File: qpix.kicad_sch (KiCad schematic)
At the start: 90 parts, among them J1 Conn_01x40, J13 DigReset, J2 Conn_01x09, J3 Conn_02x03, J4 Conn_02x03, J5 SPI, J6 Conn_02x03, J8 Conn_02x03, J9 Conn_Coaxial_Power, Q1 Q_NMOS_GSD, Q2 Q_NMOS_GSD, Q3 Q_NMOS_GSD, Q4 Q_NMOS_GSD, U1 qpix_digital

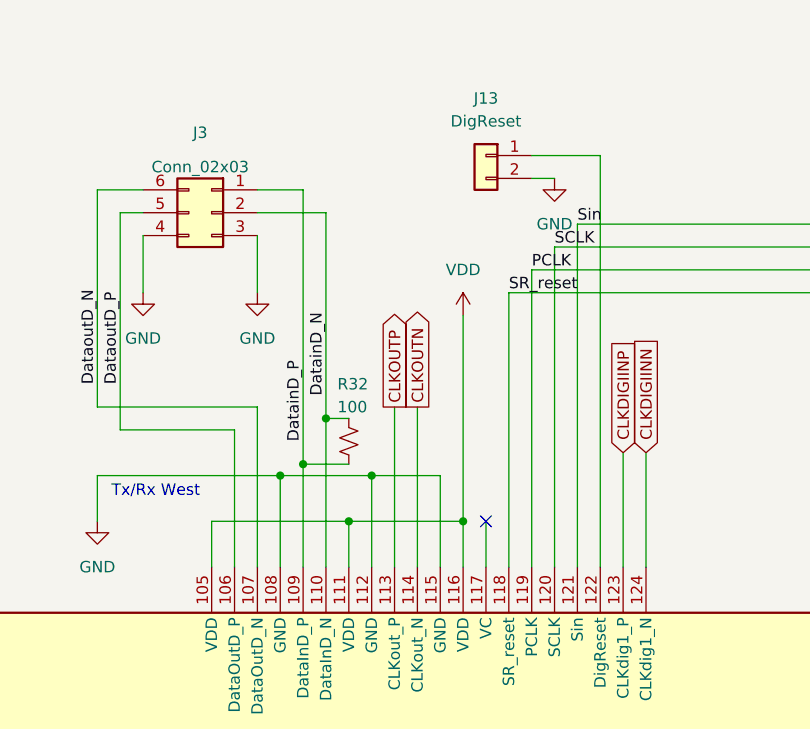
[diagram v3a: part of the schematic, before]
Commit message: connect VC DAC reference voltage to the pin header
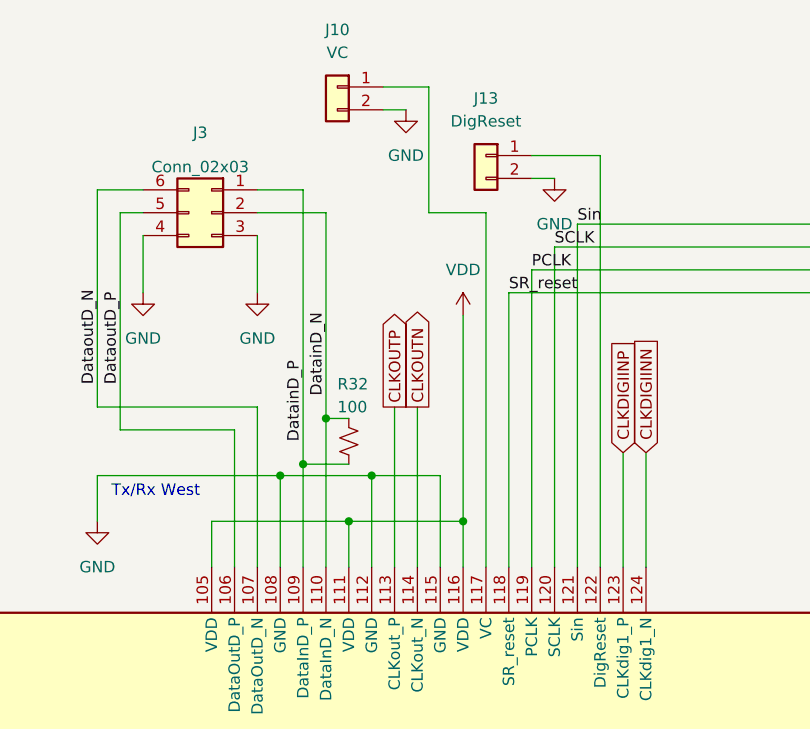
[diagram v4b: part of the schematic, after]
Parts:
- added J10: VC, Connector_PinHeader_2.54mm:PinHeader_1x02_P2.54mm_Vertical, symbol Connector_Generic:Conn_01x02
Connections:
- net GND: now also J10.2 (Pin_2)
- net at U1.117 (VC): now also J10.1 (Pin_1)
- no-connect marks 1 -> 0
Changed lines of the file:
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@@
   (junction (at 356.87 54.61) (diameter 0) (color 0 0 0 0)
   )
-  (no_connect (at 195.58 72.39))
   (wire (pts (xy 250.19 110.49) (xy 250.19 123.19))
     (stroke (width 0) (type default) (color 0 0 0 0))
@@
     (stroke (width 0) (type default) (color 0 0 0 0))
   )
+  (wire (pts (xy 184.15 26.67) (xy 186.69 26.67))
+    (stroke (width 0) (type default) (color 0 0 0 0))
+  )
   (polyline (pts (xy 276.86 104.14) (xy 406.4 104.14))
     (stroke (width 0) (type default) (color 0 0 0 0))
@@
     (stroke (width 0) (type default) (color 0 0 0 0))
   )
+  (wire (pts (xy 189.23 38.1) (xy 189.23 24.13))
+    (stroke (width 0) (type default) (color 0 0 0 0))
+  )
   (wire (pts (xy 231.14 269.24) (xy 227.33 269.24))
     (stroke (width 0) (type default) (color 0 0 0 0))
@@
     (stroke (width 0) (type default) (color 0 0 0 0))
   )
-  (wire (pts (xy 195.58 72.39) (xy 195.58 77.47))
+  (wire (pts (xy 195.58 38.1) (xy 195.58 77.47))
     (stroke (width 0) (type default) (color 0 0 0 0))
   )
@@
     (stroke (width 0) (type default) (color 0 0 0 0))
   )
+  (wire (pts (xy 195.58 38.1) (xy 189.23 38.1))
+    (stroke (width 0) (type default) (color 0 0 0 0))
+  )
   (wire (pts (xy 208.28 242.57) (xy 208.28 250.19))
     (stroke (width 0) (type default) (color 0 0 0 0))
@@
     (stroke (width 0) (type default) (color 0 0 0 0))
   )
+  (wire (pts (xy 189.23 24.13) (xy 184.15 24.13))
+    (stroke (width 0) (type default) (color 0 0 0 0))
+  )
   (wire (pts (xy 243.84 115.57) (xy 280.67 115.57))
     (stroke (width 0) (type default) (color 0 0 0 0))
@@
     (pin "2")
   )
+  (symbol (lib_id "power:GND") (at 186.69 26.67 0) (unit 1)
+    (in_bom yes) (on_board yes) (fields_autoplaced)
+    (property "Reference" "#PWR030" (id 0) (at 186.69 33.02 0)
+      (effects (font (size 1.27 1.27)) hide)
+    )
+    (property "Value" "GND" (id 1) (at 186.69 31.75 0))
+    (property "Footprint" "" (id 2) (at 186.69 26.67 0)
+      (effects (font (size 1.27 1.27)) hide)
+    )
+    (property "Datasheet" "" (id 3) (at 186.69 26.67 0)
+      (effects (font (size 1.27 1.27)) hide)
+    )
+    (pin "1")
+  )
   (symbol (lib_id "power:GND") (at 63.5 100.33 0) (unit 1)
     (in_bom yes) (on_board yes) (fields_autoplaced)
@@
     (pin "1")
   )
+  (symbol (lib_id "Connector_Generic:Conn_01x02") (at 179.07 24.13 0) (mirror y) (unit 1)
+    (in_bom yes) (on_board yes) (fields_autoplaced)
+    (property "Reference" "J10" (id 0) (at 179.07 17.78 0))
+    (property "Value" "VC" (id 1) (at 179.07 20.32 0))
+    (property "Footprint" "Connector_PinHeader_2.54mm:PinHeader_1x02_P2.54mm_Vertical" (id 2) (at 179.07 24.13 0)
+      (effects (font (size 1.27 1.27)) hide)
+    )
+    (property "Datasheet" "~" (id 3) (at 179.07 24.13 0)
+      (effects (font (size 1.27 1.27)) hide)
+    )
+    (pin "1")
+    (pin "2")
+  )
   (symbol (lib_id "Device:R_US") (at 392.43 38.1 0) (unit 1)
     (in_bom yes) (on_board yes) (fields_autoplaced)
@@
       (reference "#PWR029") (unit 1) (value "GND") (footprint "")
     )
+    (path "/7bcc8bd1-e233-4082-9758-fb375cb15776"
+      (reference "#PWR030") (unit 1) (value "GND") (footprint "")
+    )
     (path "/cfd9746d-22ce-426e-82d0-8ccddcdff8d0"
       (reference "#PWR0101") (unit 1) (value "GND") (footprint "")
@@
       (reference "J9") (unit 1) (value "Conn_Coaxial_Power") (footprint "Connector_Coaxial:SMA_Amphenol_901-144_Vertical")
     )
+    (path "/bc1cd376-db76-4c62-8e2d-505f88f0bb8b"
+      (reference "J10") (unit 1) (value "VC") (footprint "Connector_PinHeader_2.54mm:PinHeader_1x02_P2.54mm_Vertical")
+    )
     (path "/decf18ec-9000-4c82-b98e-84f22b4c4f81/96957f4e-fec0-4b85-ad7d-3f923544a411"

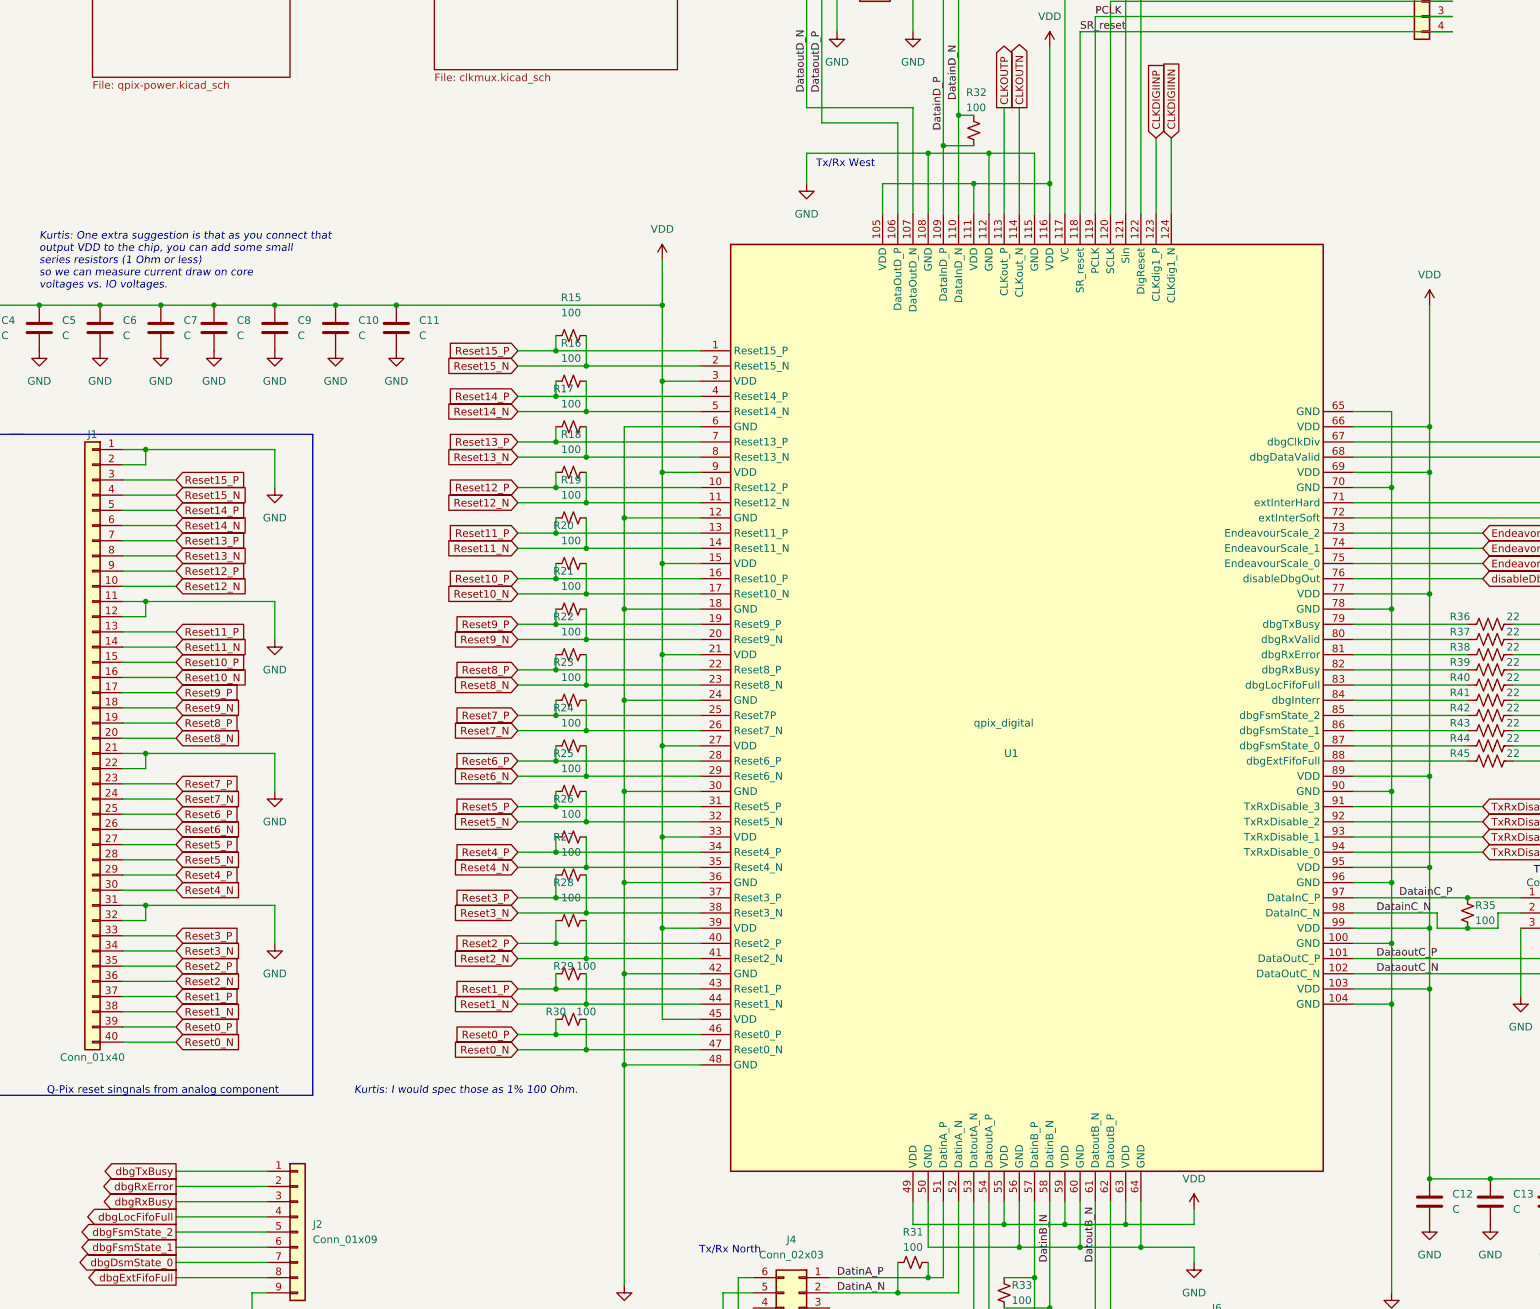
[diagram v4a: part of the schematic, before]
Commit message: fix qpix ASIC pins (65,66) -> (VDD,GND)
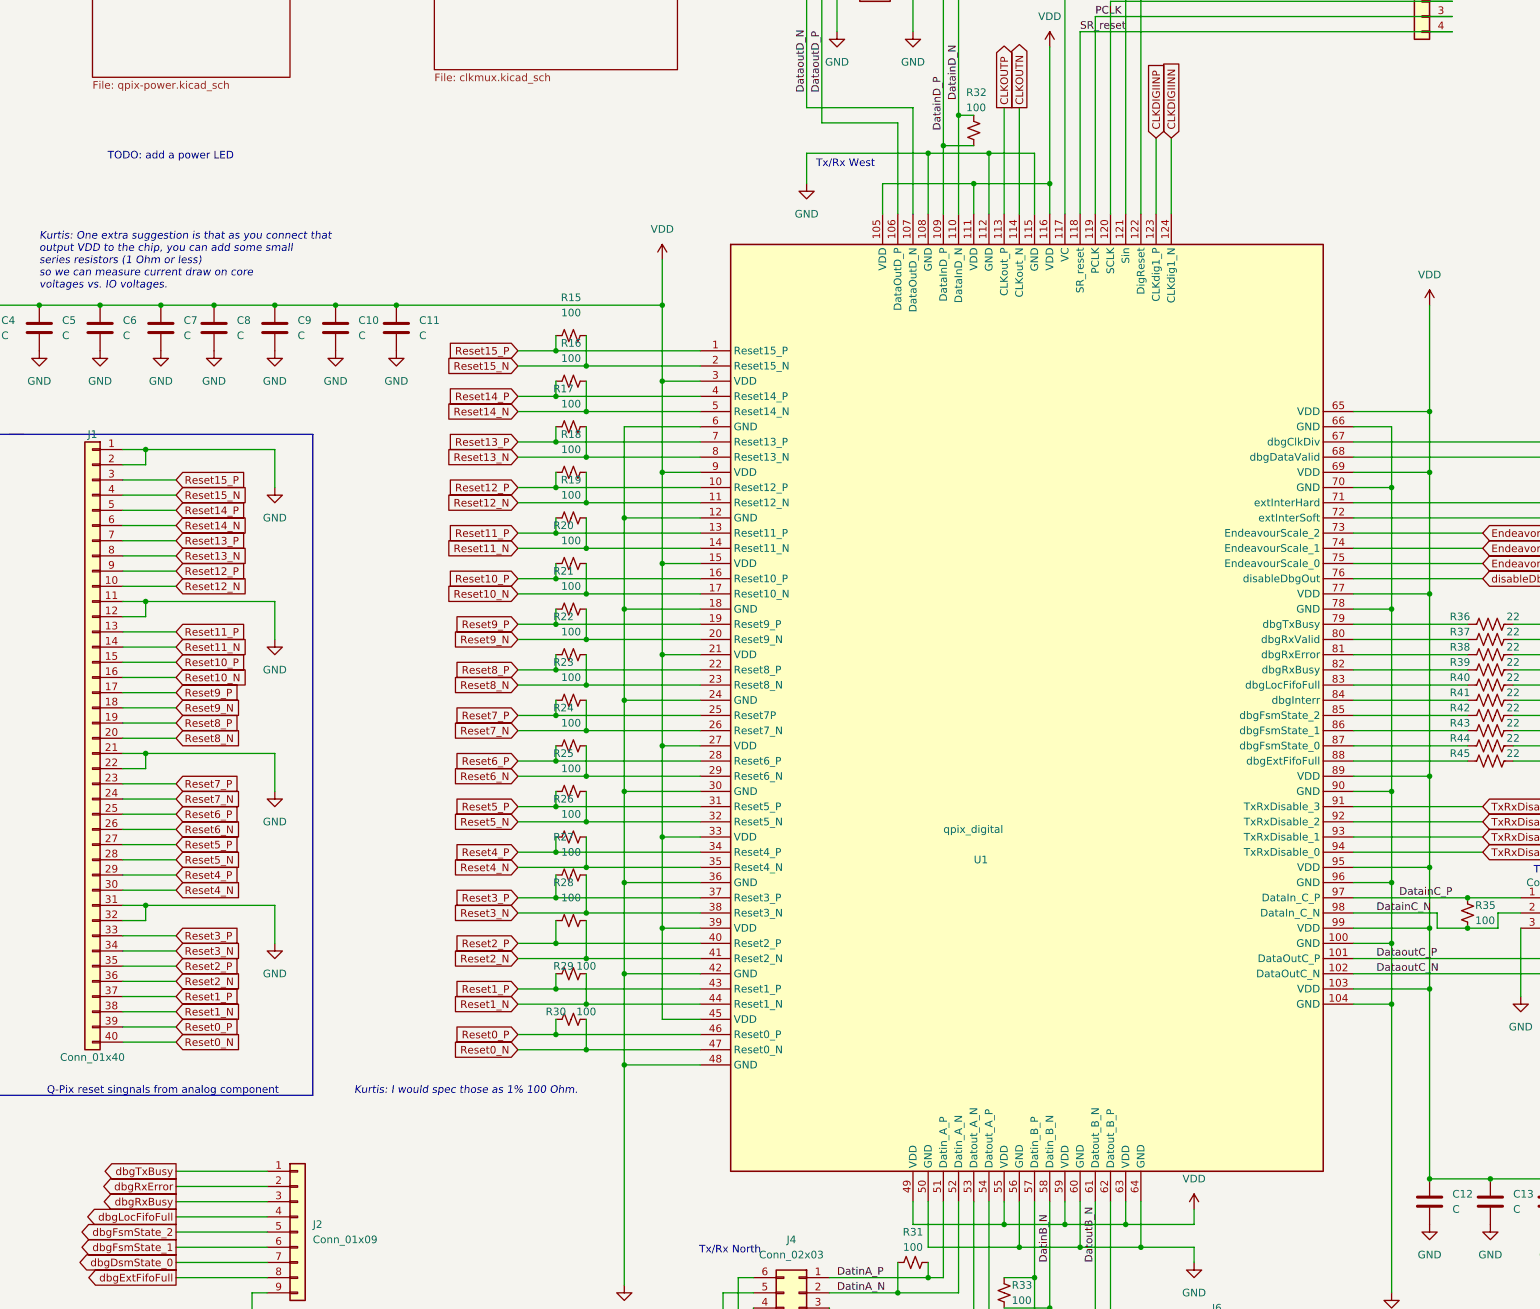
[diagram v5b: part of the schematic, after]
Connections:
- net GND: now also U1.66 (GND); no longer U1.65 (GND)
- net VDD: now also U1.65 (VDD); no longer U1.66 (VDD)
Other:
- note added: "TODO: add a power LED"
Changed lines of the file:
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@@
   (junction (at 115.57 163.83) (diameter 0) (color 0 0 0 0)
   )
+  (junction (at 256.54 110.49) (diameter 0) (color 0 0 0 0)
+  )
   (junction (at 115.57 110.49) (diameter 0) (color 0 0 0 0)
   )
@@
   (junction (at 110.49 199.39) (diameter 0) (color 0 0 0 0)
   )
-  (junction (at 250.19 123.19) (diameter 0) (color 0 0 0 0)
-  )
   (junction (at 128.27 105.41) (diameter 0) (color 0 0 0 0)
   )
@@
   (junction (at 309.88 67.31) (diameter 0) (color 0 0 0 0)
   )
-  (junction (at 256.54 113.03) (diameter 0) (color 0 0 0 0)
-  )
   (junction (at 250.19 173.99) (diameter 0) (color 0 0 0 0)
   )
@@
   (junction (at 250.19 143.51) (diameter 0) (color 0 0 0 0)
   )
+  (junction (at 250.19 123.19) (diameter 0) (color 0 0 0 0)
+  )
   (junction (at 121.92 204.47) (diameter 0) (color 0 0 0 0)
   )
@@
   (junction (at 356.87 54.61) (diameter 0) (color 0 0 0 0)
   )
-  (wire (pts (xy 250.19 110.49) (xy 250.19 123.19))
-    (stroke (width 0) (type default) (color 0 0 0 0))
-  )
   (wire (pts (xy 243.84 135.89) (xy 265.43 135.89))
     (stroke (width 0) (type default) (color 0 0 0 0))
@@
     (stroke (width 0) (type default) (color 0 0 0 0))
   )
-  (wire (pts (xy 256.54 113.03) (xy 256.54 120.65))
-    (stroke (width 0) (type default) (color 0 0 0 0))
-  )
   (wire (pts (xy 46.99 162.56) (xy 38.1 162.56))
     (stroke (width 0) (type default) (color 0 0 0 0))
@@
     (stroke (width 0) (type default) (color 0 0 0 0))
   )
-  (wire (pts (xy 243.84 110.49) (xy 250.19 110.49))
+  (wire (pts (xy 243.84 110.49) (xy 256.54 110.49))
     (stroke (width 0) (type default) (color 0 0 0 0))
   )
@@
     (stroke (width 0) (type default) (color 0 0 0 0))
   )
-  (wire (pts (xy 243.84 113.03) (xy 256.54 113.03))
-    (stroke (width 0) (type default) (color 0 0 0 0))
-  )
   (wire (pts (xy 267.97 196.85) (xy 267.97 194.31))
     (stroke (width 0) (type default) (color 0 0 0 0))
@@
     (stroke (width 0) (type default) (color 0 0 0 0))
   )
+  (wire (pts (xy 250.19 113.03) (xy 250.19 123.19))
+    (stroke (width 0) (type default) (color 0 0 0 0))
+  )
   (wire (pts (xy 115.57 120.65) (xy 115.57 125.73))
     (stroke (width 0) (type default) (color 0 0 0 0))
@@
     (stroke (width 0) (type default) (color 0 0 0 0))
   )
-  (wire (pts (xy 187.96 59.69) (xy 187.96 77.47))
-    (stroke (width 0) (type default) (color 0 0 0 0))
-  )
   (polyline (pts (xy 347.98 144.78) (xy 347.98 106.68))
     (stroke (width 0) (type default) (color 0 0 0 0))
@@
     (stroke (width 0) (type default) (color 0 0 0 0))
   )
+  (wire (pts (xy 170.18 59.69) (xy 152.4 59.69))
+    (stroke (width 0) (type default) (color 0 0 0 0))
+  )
   (wire (pts (xy 110.49 173.99) (xy 110.49 176.53))
     (stroke (width 0) (type default) (color 0 0 0 0))
@@
     (stroke (width 0) (type default) (color 0 0 0 0))
   )
+  (wire (pts (xy 256.54 110.49) (xy 256.54 120.65))
+    (stroke (width 0) (type default) (color 0 0 0 0))
+  )
   (wire (pts (xy 115.57 163.83) (xy 134.62 163.83))
     (stroke (width 0) (type default) (color 0 0 0 0))
@@
     (stroke (width 0) (type default) (color 0 0 0 0))
   )
-  (wire (pts (xy 256.54 92.71) (xy 256.54 113.03))
+  (wire (pts (xy 256.54 92.71) (xy 256.54 110.49))
     (stroke (width 0) (type default) (color 0 0 0 0))
   )
@@
     (stroke (width 0) (type default) (color 0 0 0 0))
   )
-  (wire (pts (xy 185.42 59.69) (xy 185.42 77.47))
-    (stroke (width 0) (type default) (color 0 0 0 0))
-  )
   (wire (pts (xy 128.27 120.65) (xy 128.27 105.41))
     (stroke (width 0) (type default) (color 0 0 0 0))
@@
     (stroke (width 0) (type default) (color 0 0 0 0))
   )
+  (wire (pts (xy 185.42 59.69) (xy 185.42 77.47))
+    (stroke (width 0) (type default) (color 0 0 0 0))
+  )
   (wire (pts (xy 165.1 72.39) (xy 165.1 77.47))
     (stroke (width 0) (type default) (color 0 0 0 0))
@@
     (stroke (width 0) (type default) (color 0 0 0 0))
   )
-  (wire (pts (xy 170.18 59.69) (xy 152.4 59.69))
-    (stroke (width 0) (type default) (color 0 0 0 0))
-  )
   (wire (pts (xy 256.54 196.85) (xy 256.54 207.01))
     (stroke (width 0) (type default) (color 0 0 0 0))
@@
     (stroke (width 0) (type default) (color 0 0 0 0))
   )
+  (wire (pts (xy 243.84 113.03) (xy 250.19 113.03))
+    (stroke (width 0) (type default) (color 0 0 0 0))
+  )
   (wire (pts (xy 287.02 238.76) (xy 295.91 238.76))
     (stroke (width 0) (type default) (color 0 0 0 0))
@@
     (stroke (width 0) (type default) (color 0 0 0 0))
   )
-  (wire (pts (xy 170.18 59.69) (xy 170.18 77.47))
-    (stroke (width 0) (type default) (color 0 0 0 0))
-  )
   (wire (pts (xy 115.57 171.45) (xy 134.62 171.45))
     (stroke (width 0) (type default) (color 0 0 0 0))
@@
     (stroke (width 0) (type default) (color 0 0 0 0))
   )
+  (wire (pts (xy 170.18 77.47) (xy 170.18 59.69))
+    (stroke (width 0) (type default) (color 0 0 0 0))
+  )
   (wire (pts (xy 170.18 242.57) (xy 170.18 246.38))
     (stroke (width 0) (type default) (color 0 0 0 0))
@@
     (stroke (width 0) (type default) (color 0 0 0 0))
   )
+  (wire (pts (xy 187.96 59.69) (xy 187.96 77.47))
+    (stroke (width 0) (type default) (color 0 0 0 0))
+  )
   (wire (pts (xy 128.27 120.65) (xy 134.62 120.65))
     (stroke (width 0) (type default) (color 0 0 0 0))
@@
     (effects (font (size 1.27 1.27) italic) (justify left bottom))
   )
+  (text "TODO: add a power LED" (at 35.56 68.58 0)
+    (effects (font (size 1.27 1.27)) (justify left bottom))
+  )
   (text "External interrogation\n" (at 372.11 111.76 0)
     (effects (font (size 2 2)) (justify left bottom))
@@
     (pin "2")
   )
-  (symbol (lib_id "mylib:qpix_digital") (at 139.7 82.55 0) (unit 1)
+  (symbol (lib_id "mylib:qpix_digital") (at 134.62 100.33 0) (unit 1)
     (in_bom yes) (on_board yes)
-    (property "Reference" "U1" (id 0) (at 185.42 167.64 0)
+    (property "Reference" "U1" (id 0) (at 180.34 185.42 0)
       (effects (font (size 1.27 1.27)) (justify left))
     )
-    (property "Value" "qpix_digital" (id 1) (at 180.34 162.56 0)
+    (property "Value" "qpix_digital" (id 1) (at 175.26 180.34 0)
       (effects (font (size 1.27 1.27)) (justify left))
     )
-    (property "Footprint" "qpix-digi-pcb:qpix_digi_footprint" (id 2) (at 87.63 11.43 0)
+    (property "Footprint" "qpix-digi-pcb:qpix_digi_footprint" (id 2) (at 82.55 29.21 0)
       (effects (font (size 1.27 1.27)) (justify right) hide)
     )
-    (property "Datasheet" "" (id 3) (at 87.63 16.51 0)
+    (property "Datasheet" "" (id 3) (at 82.55 34.29 0)
       (effects (font (size 1.27 1.27)) (justify right) hide)
     )
